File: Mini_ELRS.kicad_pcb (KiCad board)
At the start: 4 copper layers, 24 x 13.4 mm, 24 parts, among them J1 Conn_01x04, U1 ESP8266EX, U2 TC2014-3.3VxCTTR, U3 SX1280IMLTRT, Y1 52M, Y2 52M

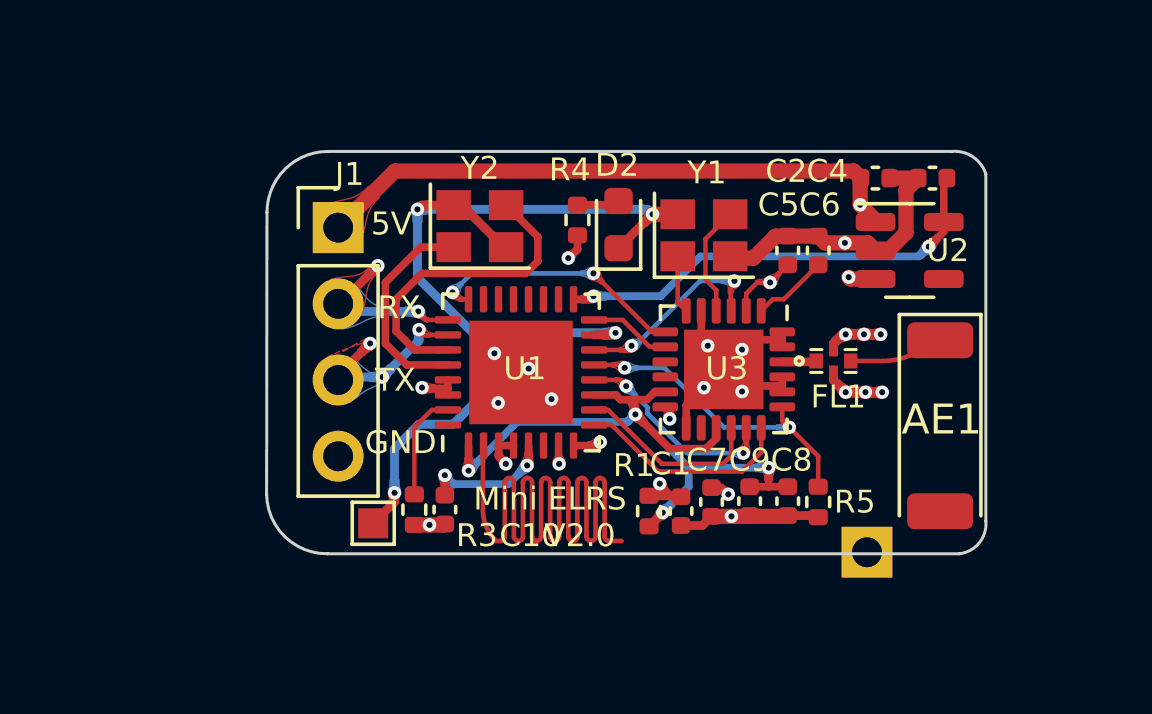
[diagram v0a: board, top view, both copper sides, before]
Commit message: add motor and servo interface
Signed-off-by: huangzzk <huangcmzzk@gmail.com>
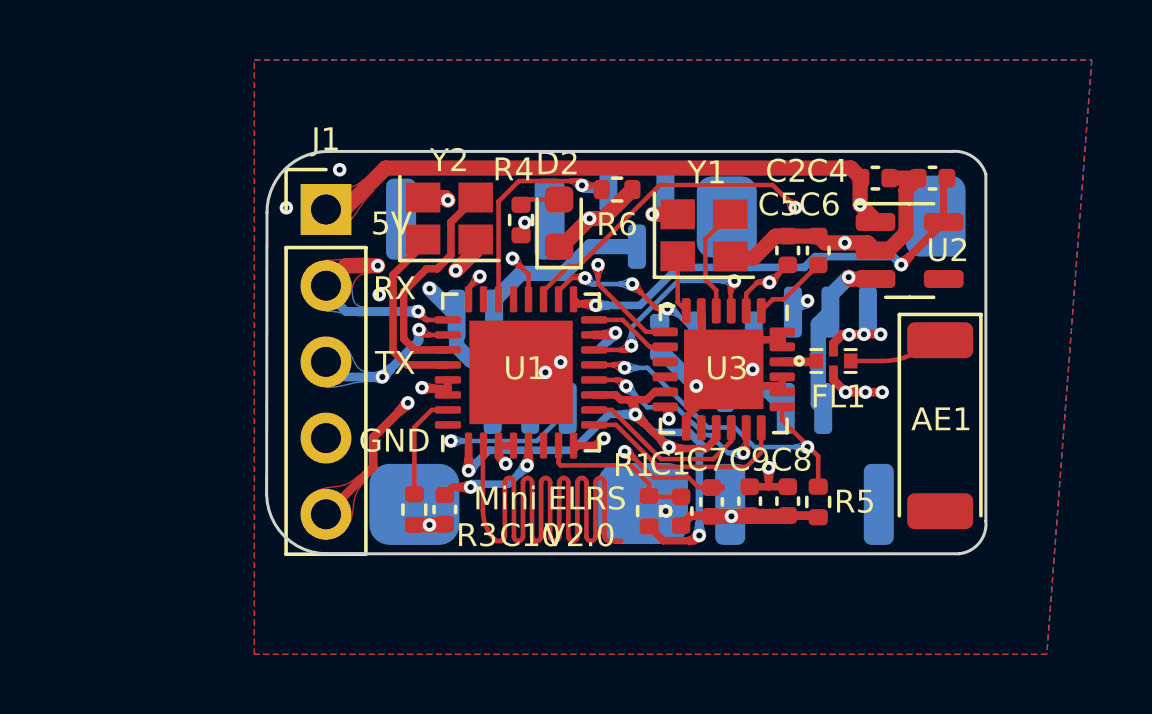
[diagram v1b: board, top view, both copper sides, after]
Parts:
- removed ?: , 
- removed TP1: TestPoint, TestPoint:TestPoint_Pad_1.0x1.0mm
- added J2: Conn_01x02_MountingPin, Connector_Molex:Molex_CLIK-Mate_502386-0270_1x02-1MP_P1.25mm_Horizontal, B.Cu at (118.4, 66.3)
- added J3: Conn_01x02_MountingPin, Connector_Molex:Molex_CLIK-Mate_502386-0270_1x02-1MP_P1.25mm_Horizontal, B.Cu at (107.4, 59.5)
- added J4: Conn_01x03_MountingPin, Connector_Molex:Molex_CLIK-Mate_502386-0370_1x03-1MP_P1.25mm_Horizontal, B.Cu at (119.3, 59.4)
- added J6: Conn_01x03_MountingPin, Connector_Molex:Molex_CLIK-Mate_502386-0370_1x03-1MP_P1.25mm_Horizontal, B.Cu at (109.3, 66.3)
- added Q1: Q_NMOS_GSD, Package_TO_SOT_SMD:SOT-23, B.Cu at (115.8, 62.9)
- added Q2: Q_NMOS_GSD, Package_TO_SOT_SMD:SOT-23, B.Cu at (112.8, 58.1)
- added R2: 10K, Resistor_SMD:R_0402_1005Metric, B.Cu at (113.6, 62.1)
- added R6: 10K, Resistor_SMD:R_0402_1005Metric, F.Cu at (112.2, 57.1)
- J1: value Conn_01x04 -> Conn_01x05; footprint Connector_PinHeader_2.54mm:PinHeader_1x04_P2.54mm_Vertical -> Connector_PinHeader_2.54mm:PinHeader_1x05_P2.54mm_Vertical
- moved D2 1.98 mm to (110.2, 58.3)
- moved R4 1.88 mm to (109.0, 58.2)
- moved Y2 1.05 mm to (106.6, 58.1)
- moved J1 0.73 mm to (102.5, 57.8)
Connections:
- U1 pad 15: Net-(U1-Pad15) -> /GPIO0
- U1 pad 18: unconnected-(U1-Pad18) -> /PWM3
- U1 pad 19: unconnected-(U1-Pad19) -> /PWM4
- U1 pad 2: unconnected-(U1-Pad2) -> /ANT
- U1 pad 20: unconnected-(U1-Pad20) -> /PWM1
- U1 pad 22: unconnected-(U1-Pad22) -> /PWM2
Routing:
- net unconnected-(U1-Pad2): track 31.0 -> 0.00 mm
- net /ANT: track 0.00 -> 31.0 mm
- net /GPIO0: track 0.00 -> 21.0 mm, vias 0 -> 2
- net +5V: track 23.5 -> 39.6 mm, vias 2 -> 3
- net /PWM4: track 0.00 -> 14.4 mm, vias 0 -> 2
- net /PWM1: track 0.00 -> 14.1 mm, vias 0 -> 2
- net Net-(U1-Pad15): track 12.5 -> 0.00 mm, vias 2 -> 0
- net GND: track 45.1 -> 33.6 mm, vias 19 -> 21
- net /PWM2: track 0.00 -> 8.05 mm, vias 0 -> 1
- net /PWM3: track 0.00 -> 6.39 mm, vias 0 -> 3
- net Net-(J3-Pad2): track 0.00 -> 6.00 mm
- net +3V3: track 51.3 -> 56.0 mm, vias 8 -> 9
- net /LED: track 8.40 -> 11.7 mm
- net Net-(U1-Pad27): track 10.6 -> 7.54 mm
- net Net-(J2-Pad2): track 0.00 -> 2.27 mm
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- added copper zone on B.Cu, net GND
- added copper zone on F.Cu, net GND
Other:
- board text added: "+"
- board text added: "G"

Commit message: fix wrong pwm pins
Signed-off-by: huangzzk <huangcmzzk@gmail.com>
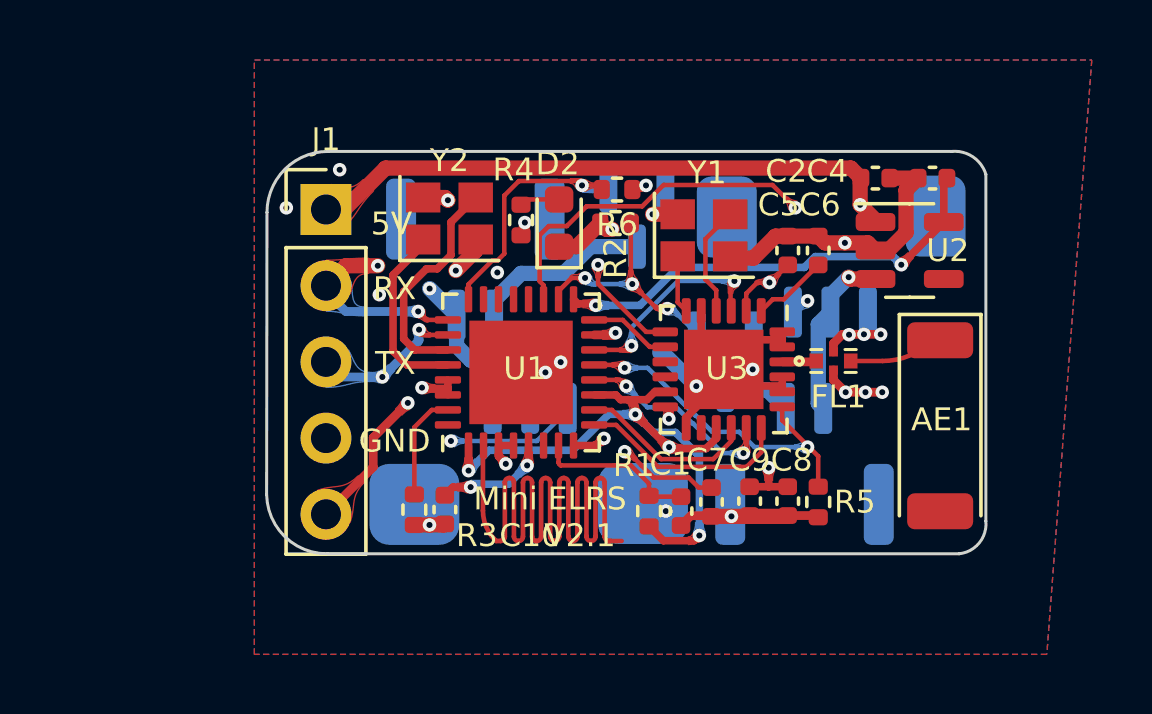
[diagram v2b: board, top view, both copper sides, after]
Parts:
- R2: moved to F.Cu
- moved R2 4.08 mm to (112.1, 58.3), turned to 180 degrees
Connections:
- J1 pad 2: /RX -> /PWM1
- U1 pad 20: /PWM1 -> unconnected-(U1-Pad20)
- U1 pad 22: /PWM2 -> unconnected-(U1-Pad22)
- U1 pad 24: /BUSY -> /PWM2
- U1 pad 25: /RX -> /PWM1
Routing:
- net /RX: track 5.88 -> 0.00 mm, vias 2 -> 0
- net /PWM3: track 6.39 -> 7.88 mm
- net /BUSY: track 9.23 -> 7.78 mm
- net /PWM4: track 14.4 -> 15.6 mm
- net /PWM1: track 14.1 -> 15.0 mm, vias 2 -> 3
- net /PWM2: track 8.05 -> 8.95 mm
- net /GPIO0: track 21.0 -> 20.2 mm
- net GND: track 33.6 -> 33.0 mm, vias 21 -> 22
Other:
- board text added: "Mini ELRS V2.1"
- board text removed: "Mini ELRS V2.0"

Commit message: update
Signed-off-by: huangzzk <huangcmzzk@gmail.com>
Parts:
- moved R1 1.79 mm to (115.0, 67.7)
- moved C1 1.63 mm to (115.9, 67.7)
- moved C7 1.58 mm to (116.9, 67.5)
- moved C9 1.22 mm to (117.8, 67.5)
- moved C8 0.91 mm to (118.8, 67.5)
- moved R5 0.86 mm to (119.7, 67.6)
- moved C10 0.05 mm to (106.4, 67.8)
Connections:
- U1 pad 16: /DIO1 -> /PWM3
- U1 pad 18: /PWM3 -> /DIO1
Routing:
- net /BUSY: track 7.78 -> 0.00 mm, vias 2 -> 0
- net GND: track 33.0 -> 27.6 mm, vias 22 -> 21
- net /DIO1: track 2.74 -> 5.42 mm, vias 0 -> 2
- net Net-(C5-Pad1): track 14.1 -> 15.6 mm
- net Net-(C1-Pad1): track 5.37 -> 6.65 mm
- net +3V3: track 55.7 -> 54.5 mm, vias 9 -> 10
- net /PWM3: track 7.88 -> 6.83 mm, vias 3 -> 2
- net /ANT: track 31.0 -> 31.6 mm

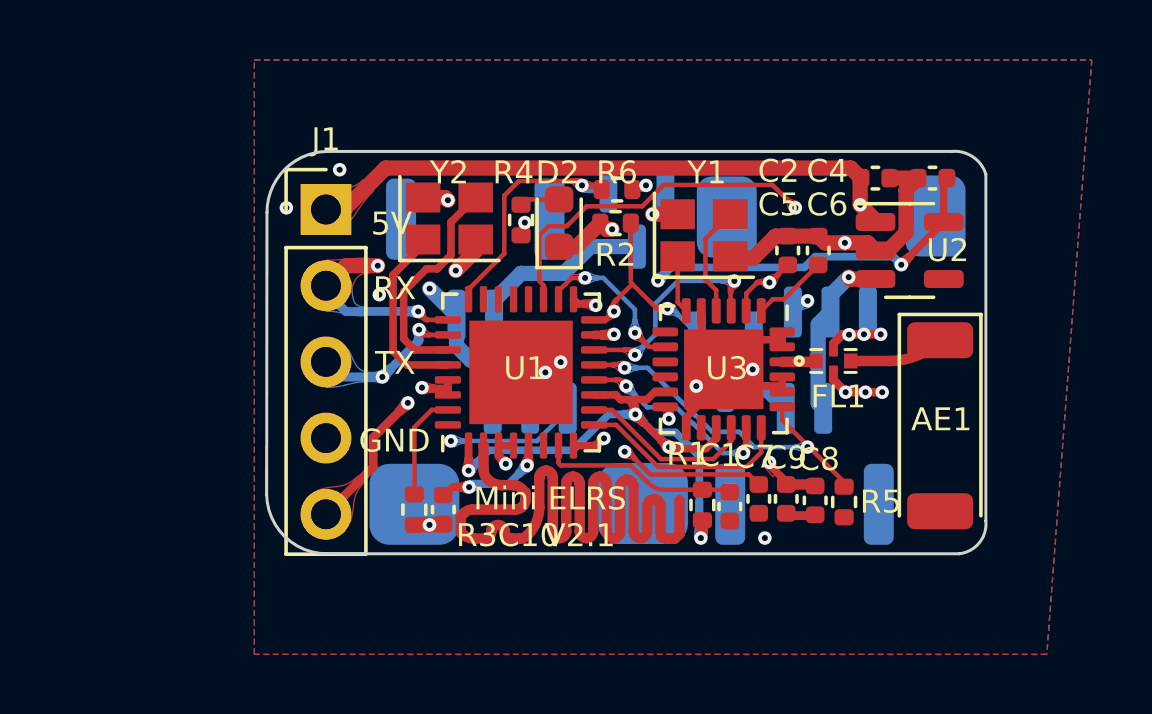
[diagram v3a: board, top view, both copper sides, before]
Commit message: v2.2 add diode in motor interface
Signed-off-by: huangzzk <huangcmzzk@gmail.com>
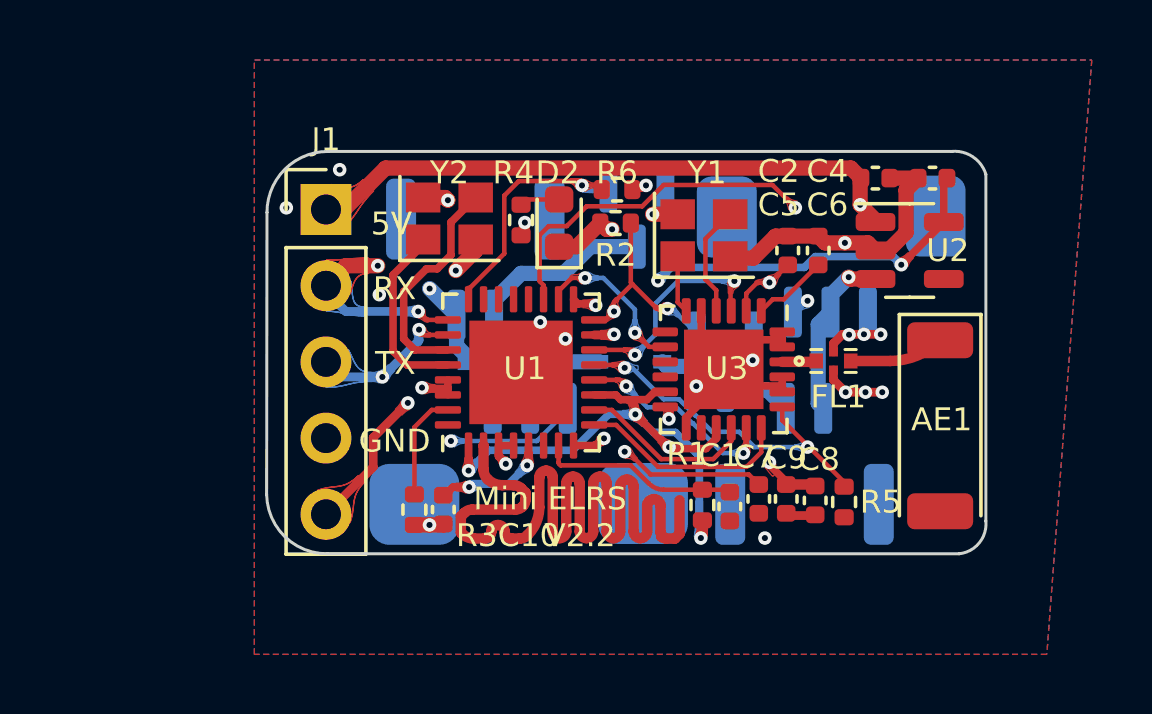
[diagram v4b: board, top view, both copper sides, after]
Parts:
- added D1: D, Diode_SMD:D_SOD-323, B.Cu at (112.6, 62.9)
- added D3: D, Diode_SMD:D_SOD-323, B.Cu at (108.2, 62.9)
- U1: value ESP8266EX -> ESP8285
- Y2: value 52M -> 26M
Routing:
- net +5V: track 39.2 -> 42.3 mm
- net Net-(J2-Pad2): track 2.27 -> 4.87 mm
- net Net-(J3-Pad2): track 6.00 -> 8.01 mm
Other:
- board text added: "Mini ELRS V2.2"
- board text removed: "Mini ELRS V2.1"

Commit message: 3.0 add imu 42670
Signed-off-by: huangzzk <huangcmzzk@gmail.com>
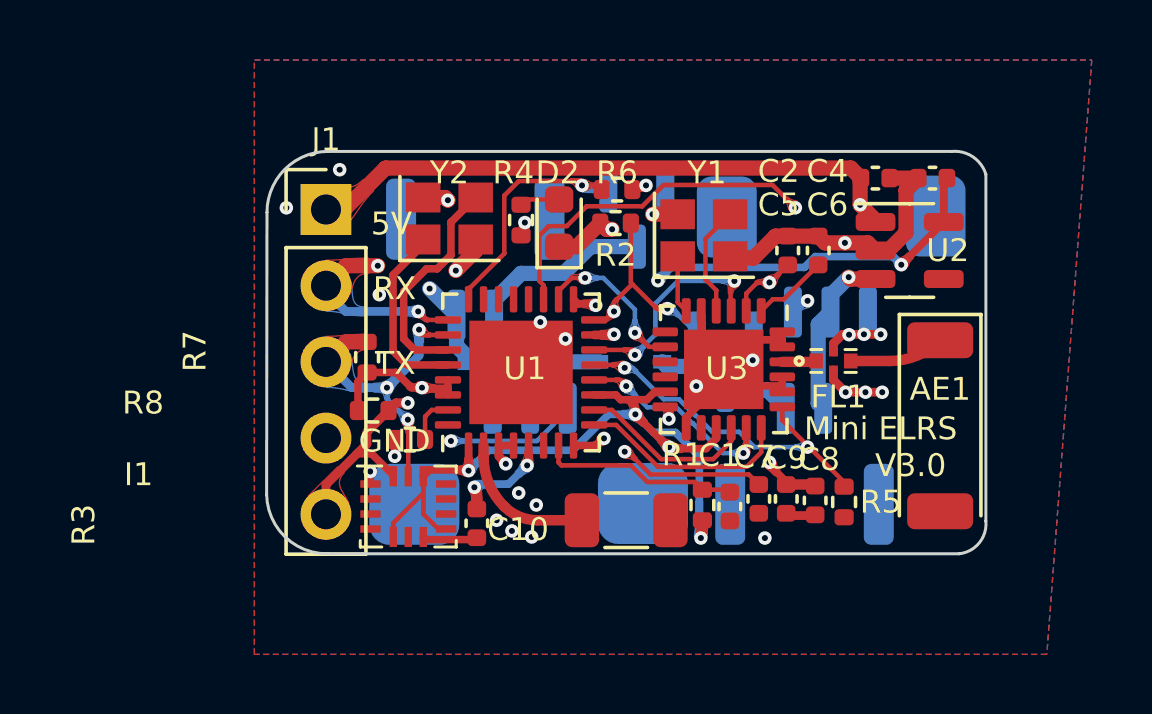
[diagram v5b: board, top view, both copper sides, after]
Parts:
- added AE2: Antenna, Capacitor_SMD:C_1206_3216Metric, F.Cu at (112.5, 68.2)
- added I1: ICM20600, Package_LGA:Bosch_LGA-14_3x2.5mm_P0.5mm, F.Cu at (105.2, 67.7)
- added R7: 10K, Resistor_SMD:R_0402_1005Metric, F.Cu at (103.8, 62.7)
- added R8: 10K, Resistor_SMD:R_0402_1005Metric, F.Cu at (104.0, 64.5)
- moved R3 2.34 mm to (105.3, 65.5), turned to 0 degrees
- moved C10 1.21 mm to (107.5, 68.3)
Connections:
- U1 pad 2: /ANT -> Net-(U1-Pad2)
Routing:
- net /ANT: track 31.6 -> 0.00 mm
- net +3V3: track 54.5 -> 63.7 mm
- net /TX: track 5.21 -> 10.7 mm, vias 2 -> 3
- net Net-(U1-Pad2): track 0.00 -> 4.91 mm
- net /GPIO0: track 20.1 -> 22.0 mm
- net Net-(R3-Pad2): track 3.59 -> 1.72 mm
- net GND: track 27.6 -> 29.4 mm, vias 21 -> 27
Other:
- board text added: "Mini ELRS V3.0"
- board text removed: "Mini ELRS V2.2"
